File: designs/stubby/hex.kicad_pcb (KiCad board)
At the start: 2 copper layers, 50 x 50 mm, 35 parts, among them IC1 ATMEGA1284P-P, K1 XTAL, K2 REGUL, P1 PROG, P2 BATT (4.8V-6V), P3 CONN_8, SW1 DPDT, X1 XBee (Sparkfun Breakout)

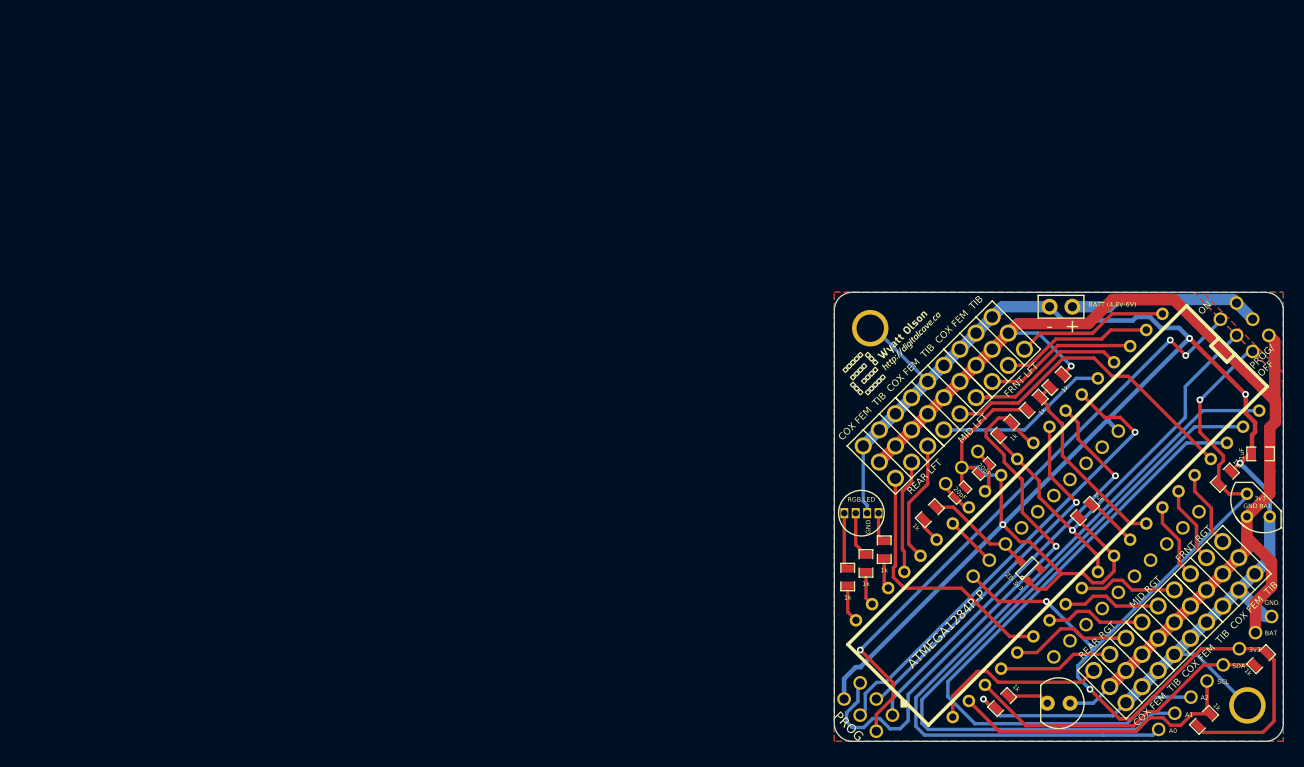
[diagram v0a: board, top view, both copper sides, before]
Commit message: Moved a few components around... trying to keep things off the back and out from under the DIP chip as much as possible.  Currently only crystal's caps are on the back.  Adjusting silk screen to better fit components.
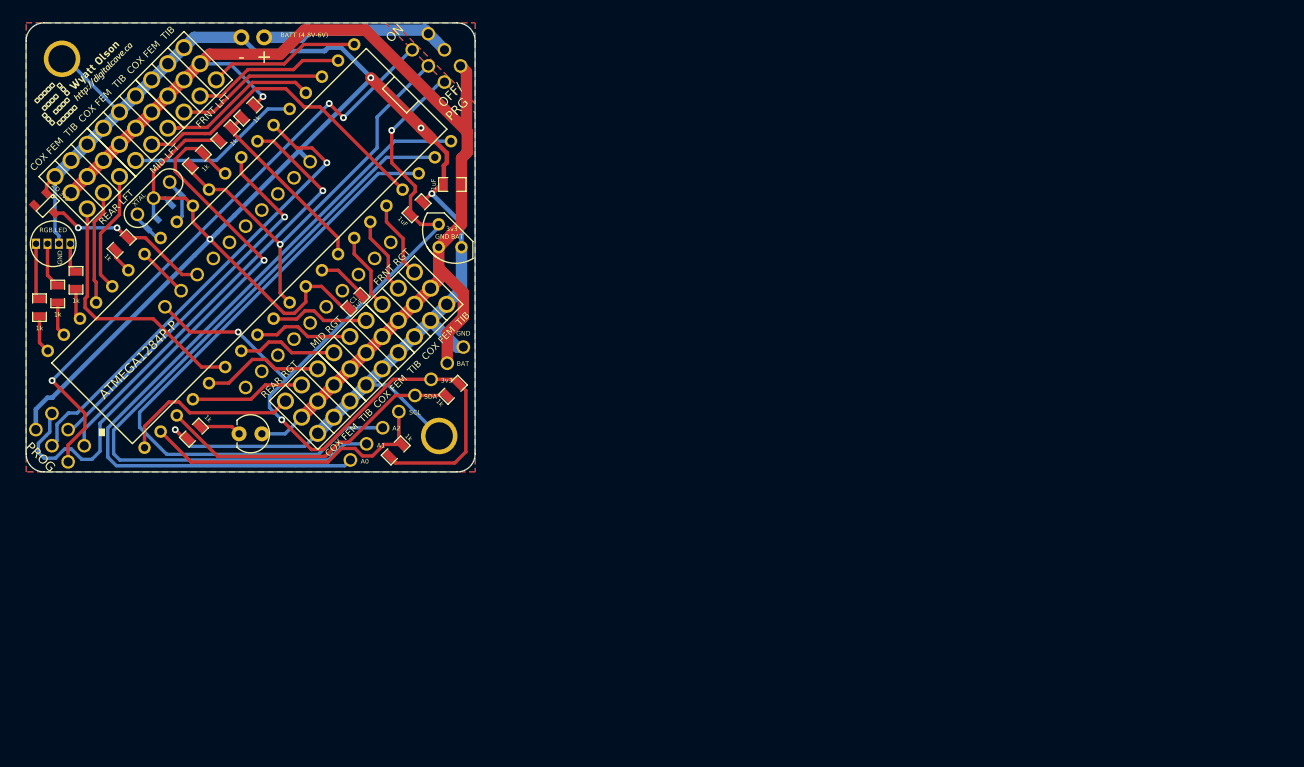
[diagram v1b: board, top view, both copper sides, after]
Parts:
- C4, C5: moved to B.Cu
- K1: moved to F.Cu
- moved ZD1 116.3 mm to (37.4, 35.4), turned to 225 degrees
- moved C2 94.9 mm to (82.5, 33.0)
- moved P2 94.9 mm to (60.2, 16.6)
- moved R3 94.9 mm to (57.2, 27.4)
- moved R4 94.9 mm to (40.6, 43.7)
- moved S5 94.9 mm to (43.6, 31.2)
- moved 1PIN 94.9 mm to (81.0, 61.0)
- moved 1PIN 94.9 mm to (39.0, 19.0)
- moved C4 94.9 mm to (51.7, 34.6)
- moved C5 94.9 mm to (49.0, 37.3)
- moved D1 94.9 mm to (60.0, 60.8)
- moved K1 94.9 mm to (49.2, 34.5)
- moved L1 94.9 mm to (38.0, 39.6)
- moved P1 94.9 mm to (38.8, 61.2)
- moved P3 94.9 mm to (78.3, 56.5)
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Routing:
- net GND: track 262.4 -> 255.5 mm
- net AVR_TX: track 12.0 -> 18.7 mm, vias 0 -> 2
- net MISO: track 46.6 -> 49.0 mm
- net RESET: track 62.8 -> 64.9 mm
- net SCK: track 41.3 -> 42.8 mm
- net VCC_AVR: track 49.1 -> 47.6 mm
- net ADC_BATTERY_METER: track 21.7 -> 20.6 mm
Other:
- board text added: "OFF/ PRG"
- board text removed: "PROG/ OFF"

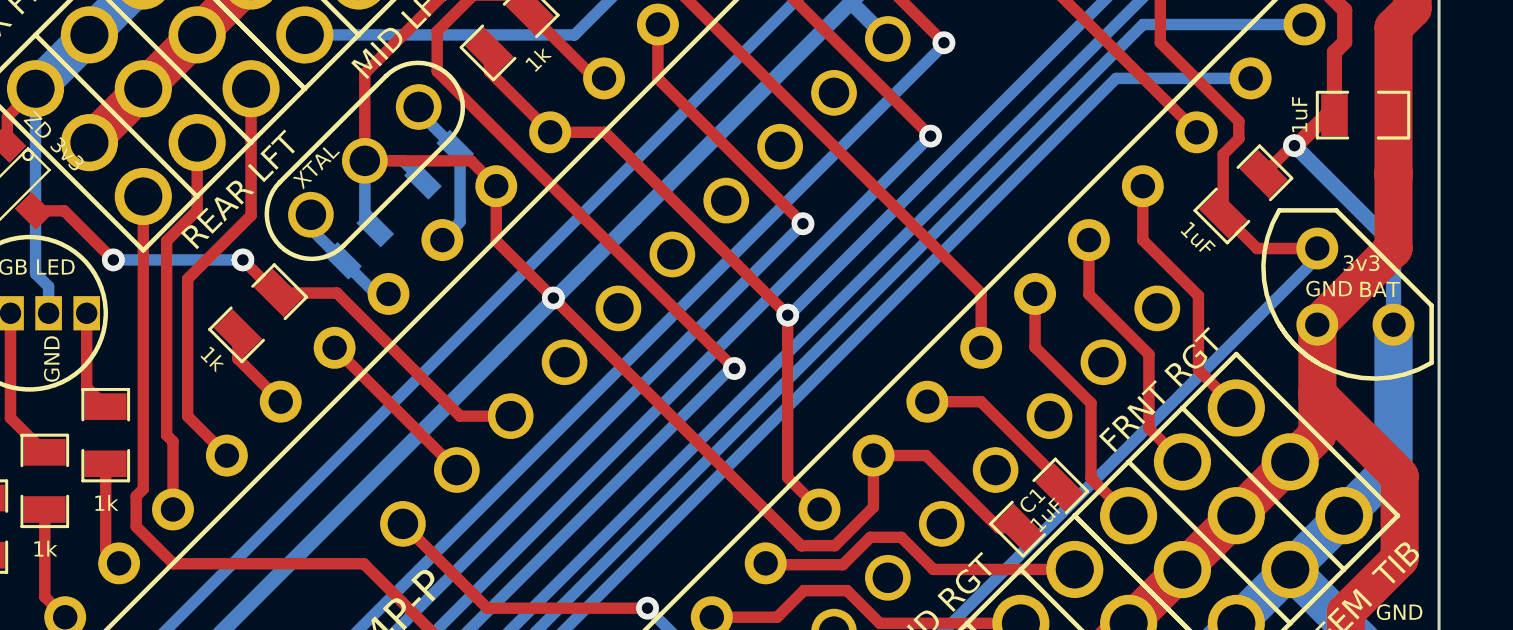
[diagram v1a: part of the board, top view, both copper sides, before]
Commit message: Moved resistor away from crystal for better fit
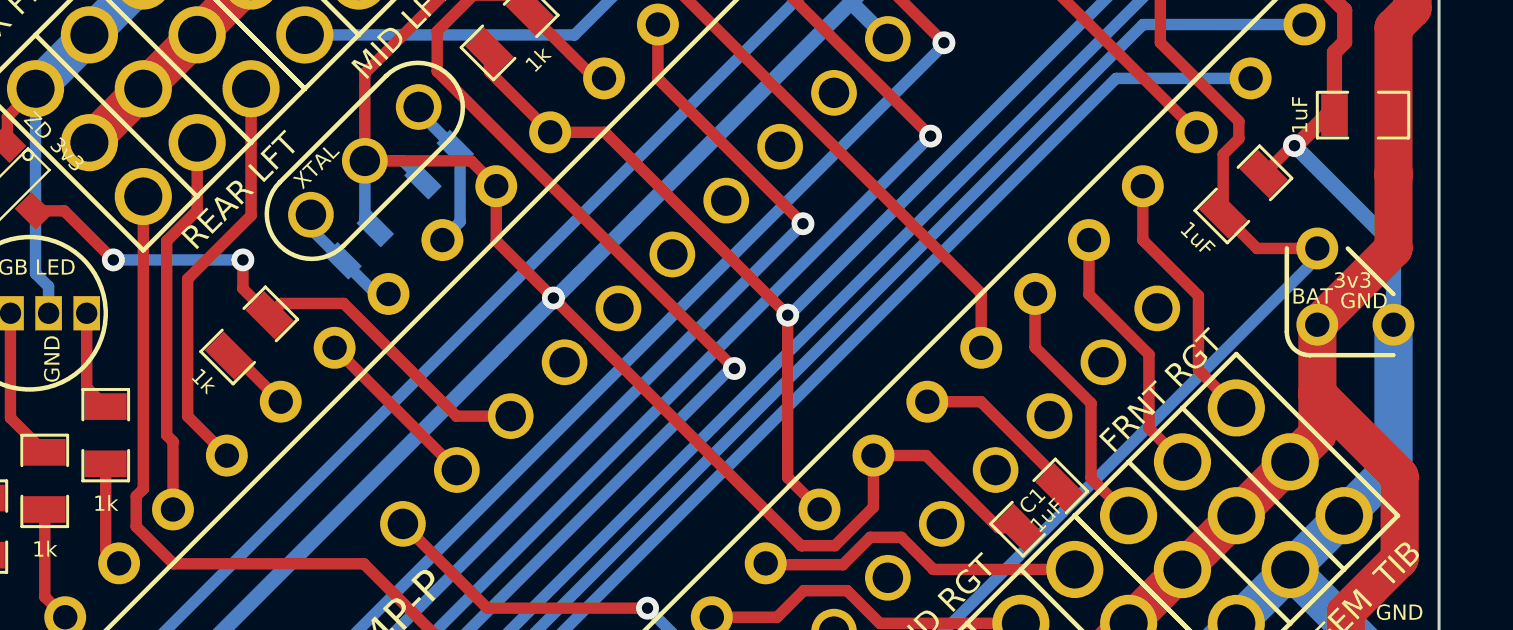
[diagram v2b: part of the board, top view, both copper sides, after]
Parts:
- moved R9 0.80 mm to (45.3, 40.3)
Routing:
- net AVR_TX: track 18.7 -> 19.6 mm
- net N-0000033: track 2.87 -> 2.36 mm
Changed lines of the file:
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@@
-(kicad_pcb (version 3) (host pcbnew "(2014-01-10 BZR 4027)-stable")
+(kicad_pcb (version 3) (host pcbnew "(2013-dec-23)-stable")
   (general
     (links 119)
@@
     (thickness 1.6)
     (drawings 27)
-    (tracks 438)
+    (tracks 439)
     (zones 0)
     (modules 35)
@@
     (pad_to_mask_clearance 0)
     (aux_axis_origin 0 0)
-    (visible_elements FFFFBFBF)
+    (visible_elements FFFFFFBF)
     (pcbplotparams
       (layerselection 284196865)
@@
     (add_net XTAL2)
   )
+  (module TO92 (layer F.Cu)
+    (at 82.212 38.707 90)
+    (descr "Transistor TO92 brochage type BC237")
+    (tags "TR TO92")
+    (fp_text reference K2 (at -1.27 3.81 90) (layer F.SilkS) hide
+      (effects (font (size 1.016 1.016) (thickness 0.2032)))
+    )
+    (fp_text value REGUL (at -0.1016 -0.1778 180) (layer F.SilkS) hide
+      (effects (font (size 0.508 0.508) (thickness 0.127)))
+    )
+    (fp_arc (start -1.524 -1.524) (end -2.286 -1.524) (angle 90) (layer F.SilkS) (width 0.15))
+    (fp_line (start -1.524 -2.286) (end 1.27 -2.286) (layer F.SilkS) (width 0.15))
+    (fp_line (start -2.286 -1.524) (end -2.286 1.27) (layer F.SilkS) (width 0.15))
+    (fp_line (start 1.27 -0.254) (end -0.254 1.27) (layer F.SilkS) (width 0.15))
+    (pad 1 thru_hole circle (at -1.27 1.27 90) (size 1.397 1.397) (drill 0.8128)
+      (layers *.Cu *.Mask F.SilkS)
+      (net 9 GND)
+    )
+    (pad 2 thru_hole circle (at -1.27 -1.27 90) (size 1.397 1.397) (drill 0.8128)
+      (layers *.Cu *.Mask F.SilkS)
+      (net 42 SWITCHED_BATTERY)
+    )
+    (pad 3 thru_hole circle (at 1.27 -1.27 90) (size 1.397 1.397) (drill 0.8128)
+      (layers *.Cu *.Mask F.SilkS)
+      (net 43 VCC_3v3)
+    )
+    (model discret/to98.wrl
+      (at (xyz 0 0 0))
+      (scale (xyz 1 1 1))
+      (rotate (xyz 0 0 0))
+    )
+  )
   (module LED-5MM (layer F.Cu)
     (at 59.987 60.7542 180)
@@
   )
   (module SM0805 (layer F.Cu)
-    (at 45.636 39.596 45)
+    (at 45.339 40.3352 45)
     (attr smd)
     (fp_text reference R9 (at 0 -0.3175 45) (layer F.SilkS) hide
@@
     )
   )
-  (module TO92 (layer F.Cu)
-    (at 82.212 38.707 90)
-    (descr "Transistor TO92 brochage type BC237")
-    (tags "TR TO92")
-    (fp_text reference K2 (at -1.27 3.81 90) (layer F.SilkS) hide
-      (effects (font (size 1.016 1.016) (thickness 0.2032)))
-    )
-    (fp_text value REGUL (at -0.1016 -0.1778 180) (layer F.SilkS) hide
-      (effects (font (size 0.508 0.508) (thickness 0.127)))
-    )
-    (fp_line (start 2.54 -2.54) (end 2.54 -0.635) (layer F.SilkS) (width 0.15))
-    (fp_line (start 2.54 -0.635) (end -0.635 2.54) (layer F.SilkS) (width 0.15))
-    (fp_line (start -0.635 2.54) (end -2.54 2.54) (layer F.SilkS) (width 0.15))
-    (fp_arc (start 0.635 0.635) (end -2.54 2.54) (angle 90) (layer F.SilkS) (width 0.15))
-    (fp_arc (start 0.635 0.635) (end -2.54 -1.27) (angle 90) (layer F.SilkS) (width 0.15))
-    (pad 1 thru_hole circle (at -1.27 1.27 90) (size 1.397 1.397) (drill 0.8128)
-      (layers *.Cu *.Mask F.SilkS)
-      (net 9 GND)
-    )
-    (pad 2 thru_hole circle (at -1.27 -1.27 90) (size 1.397 1.397) (drill 0.8128)
-      (layers *.Cu *.Mask F.SilkS)
-      (net 42 SWITCHED_BATTERY)
-    )
-    (pad 3 thru_hole circle (at 1.27 -1.27 90) (size 1.397 1.397) (drill 0.8128)
-      (layers *.Cu *.Mask F.SilkS)
-      (net 43 VCC_3v3)
-    )
-    (model discret/to98.wrl
-      (at (xyz 0 0 0))
-      (scale (xyz 1 1 1))
-      (rotate (xyz 0 0 0))
-    )
-  )
   (module 1pin (layer F.Cu)
     (at 39 19)
@@
     (effects (font (size 0.508 0.508) (thickness 0.127)))
   )
-  (gr_text BAT (at 82.9994 38.8213) (layer F.SilkS)
+  (gr_text BAT (at 80.772 39.0398) (layer F.SilkS)
     (effects (font (size 0.508 0.508) (thickness 0.127)))
   )
-  (gr_text 3v3 (at 82.4152 37.945) (layer F.SilkS)
+  (gr_text 3v3 (at 82.1182 38.5064) (layer F.SilkS)
     (effects (font (size 0.508 0.508) (thickness 0.127)))
   )
-  (gr_text GND (at 81.3357 38.7959) (layer F.SilkS)
+  (gr_text GND (at 82.4992 39.1922) (layer F.SilkS)
     (effects (font (size 0.508 0.508) (thickness 0.127)))
   )
@@
   (segment (start 48.185667 40.748026) (end 48.185668 40.748026) (width 0.381) (layer F.Cu) (net 6))
   (segment (start 48.185668 40.748026) (end 52.258693 44.821051) (width 0.381) (layer F.Cu) (net 6))
+  (segment (start 45.128 37.818) (end 45.128 38.777162) (width 0.381) (layer F.Cu) (net 7))
+  (segment (start 45.128 38.777162) (end 46.012519 39.661681) (width 0.381) (layer F.Cu) (net 7))
+  (segment (start 54.054744 43.025) (end 52.2452 43.025) (width 0.381) (layer F.Cu) (net 7))
+  (segment (start 52.2452 43.025) (end 48.4886 39.2684) (width 0.381) (layer F.Cu) (net 7))
+  (segment (start 48.4886 39.2684) (end 46.4058 39.2684) (width 0.381) (layer F.Cu) (net 7))
+  (segment (start 46.4058 39.2684) (end 46.012519 39.661681) (width 0.381) (layer F.Cu) (net 7))
   (segment (start 38.15869 36.18269) (end 39.17469 36.18269) (width 0.381) (layer F.Cu) (net 7))
-  (segment (start 46.232481 38.922481) (end 46.309519 38.922481) (width 0.381) (layer F.Cu) (net 7))
-  (segment (start 45.128 37.818) (end 46.232481 38.922481) (width 0.381) (layer F.Cu) (net 7))
   (via (at 45.128 37.818) (size 0.762) (layers F.Cu B.Cu) (net 7))
   (segment (start 40.81 37.818) (end 45.128 37.818) (width 0.381) (layer B.Cu) (net 7))
   (via (at 40.81 37.818) (size 0.762) (layers F.Cu B.Cu) (net 7))
   (segment (start 39.17469 36.18269) (end 40.81 37.818) (width 0.381) (layer F.Cu) (net 7))
-  (segment (start 46.309519 38.922481) (end 48.264481 38.922481) (width 0.381) (layer F.Cu) (net 7))
-  (segment (start 48.264481 38.922481) (end 52.367 43.025) (width 0.381) (layer F.Cu) (net 7))
-  (segment (start 52.367 43.025) (end 54.054744 43.025) (width 0.381) (layer F.Cu) (net 7))
   (segment (start 79.789974 16.155203) (end 79.789975 16.155203) (width 1.27) (layer B.Cu) (net 8))
   (segment (start 79.789975 16.155203) (end 81.586026 17.996974) (width 1.27) (layer B.Cu) (net 8))
@@
   (segment (start 54.361319 59.953681) (end 57.916481 59.953681) (width 0.381) (layer F.Cu) (net 20))
   (segment (start 57.916481 59.953681) (end 58.717 60.7542) (width 0.381) (layer F.Cu) (net 20))
-  (segment (start 44.962481 40.269519) (end 44.962481 41.116942) (width 0.381) (layer F.Cu) (net 21))
-  (segment (start 44.962481 41.116942) (end 46.389616 42.544077) (width 0.381) (layer F.Cu) (net 21))
+  (segment (start 44.665481 41.008719) (end 44.854258 41.008719) (width 0.381) (layer F.Cu) (net 21))
+  (segment (start 44.854258 41.008719) (end 46.389616 42.544077) (width 0.381) (layer F.Cu) (net 21))
   (segment (start 52.577549 24.934528) (end 55.852472 24.934528) (width 0.381) (layer F.Cu) (net 22))
   (segment (start 67.877771 20.927002) (end 67.942231 20.991462) (width 0.381) (layer F.Cu) (net 22))

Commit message: A couple more minor component movements; cleaning up silk screen.  Ready for ordering, I think...
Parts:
- moved ZD1 6.26 mm to (42.8, 38.5), turned to 90 degrees
- moved R9 3.26 mm to (42.6, 42.1), turned to 90 degrees
- moved R1 1.32 mm to (55.1, 29.5)
- moved R3 0.92 mm to (57.9, 26.8)
- moved R2 0.81 mm to (60.4, 24.3)
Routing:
- net GND: track 255.5 -> 262.9 mm
- net AVR_TX: track 19.6 -> 16.8 mm, vias 2 -> 0
- net SWITCHED_BATTERY: track 132.8 -> 135.3 mm
- net N-0000033: track 2.36 -> 4.01 mm
- net RESET: track 64.9 -> 66.4 mm
- net PWM14: track 13.6 -> 12.6 mm
- net PWM12: track 29.4 -> 29.7 mm, vias 0 -> 1
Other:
- board text added: "OFF/PROG"
- board text removed: "OFF/ PRG"
